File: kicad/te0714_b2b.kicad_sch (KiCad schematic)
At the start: 3 parts

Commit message: WIP
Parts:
- added R1, R11, R12, R13, R14: 10k, Resistor_SMD:R_0603_1608Metric, symbol Device:R_Small
- J5, J6: renamed from J?; footprint MODULE -> Connector_Samtec:Samtec_LSHM-150-xx.x-x-DV-S_2x50-1SH_P0.50mm_Vertical
- gave numbers to parts that had none: 1
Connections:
- net GND: now also J5.SH, J6.SH
- net VCCIO_0: now also R1.2, R11.2, R12.2, R13.2, R14.1
- net B14_L0 renamed IO_L0_14
- net B14_L10_N renamed IO_L10N_14
- net B14_L10_P renamed IO_L10P_14
- net B14_L11_N renamed IO_L11N_14
- net B14_L11_P renamed IO_L11P_14
- net B14_L12_N renamed IO_L12N_14
- net B14_L12_P renamed IO_L12P_14
- net B14_L13_N renamed IO_L13N_14
- net B14_L13_P renamed IO_L13P_14
- net B14_L14_N renamed IO_L14N_14
- net B14_L14_P renamed IO_L14P_14
- net B14_L15_N renamed IO_L15N_14
- net B14_L15_P renamed IO_L15P_14
- net B14_L16_N renamed IO_L16N_14
- net B14_L16_P renamed IO_L16P_14
- net B14_L17_N renamed IO_L17N_14
- net B14_L17_P renamed IO_L17P_14
- net B14_L18_N renamed IO_L18N_14
- net B14_L18_P renamed IO_L18P_14
- net B14_L19_N renamed IO_L19N_14
- net B14_L19_P renamed IO_L19P_14
- net B14_L20_N renamed IO_L20N_14
- net B14_L20_P renamed IO_L20P_14
- net B14_L21_N renamed IO_L21N_14
- net B14_L21_P renamed IO_L21P_14
- net B14_L22_N renamed IO_L22N_14
- net B14_L22_P renamed IO_L22P_14
- net B14_L23_N renamed IO_L23N_14
- net B14_L23_P renamed IO_L23P_14
- net B14_L24_N renamed IO_L24N_14
- net B14_L24_P renamed IO_L24P_14
- net B14_L25 renamed IO_L25_14
- net B14_L4_N renamed IO_L4N_14
- net B14_L4_P renamed IO_L4P_14
- net B14_L5_N renamed IO_L5N_14
- net B14_L5_P renamed IO_L5P_14
- net B14_L7_N renamed IO_L7N_14
- net B14_L7_P renamed IO_L7P_14
- net B14_L8_N renamed IO_L8N_14
- net B14_L8_P renamed IO_L8P_14
- net B14_L9_N renamed IO_L9N_14
- net B14_L9_P renamed IO_L9P_14
- net B15_L10_N renamed IO_L10N_15
- net B15_L10_P renamed IO_L10P_15
- net B15_L11_N renamed IO_L11N_15
- net B15_L11_P renamed IO_L11P_15
- net B15_L12_N renamed IO_L12N_15
- net B15_L12_P renamed IO_L12P_15
- net B15_L13_N renamed IO_L13N_15
- net B15_L13_P renamed IO_L13P_15
- net B15_L14_N renamed IO_L14N_15
- net B15_L14_P renamed IO_L14P_15
- net B15_L15_N renamed IO_L15N_15
- net B15_L15_P renamed IO_L15P_15
- net B15_L16_N renamed IO_L16N_15
- net B15_L16_P renamed IO_L16P_15
- net B15_L17_N renamed IO_L17N_15
- net B15_L17_P renamed IO_L17P_15
- net B15_L18_N renamed IO_L18N_15
- net B15_L18_P renamed IO_L18P_15
- net B15_L19_N renamed IO_L19N_15
- net B15_L19_P renamed IO_L19P_15
- net B15_L1_N renamed IO_L1N_15
- net B15_L1_P renamed IO_L1P_15
- net B15_L20_N renamed IO_L20N_15
- net B15_L20_P renamed IO_L20P_15
- net B15_L21_N renamed IO_L21N_15
- net B15_L21_P renamed IO_L21P_15
- net B15_L22_N renamed IO_L22N_15
- net B15_L22_P renamed IO_L22P_15
- net B15_L23_N renamed IO_L23N_15
- net B15_L23_P renamed IO_L23P_15
- net B15_L24_N renamed IO_L24N_15
- net B15_L24_P renamed IO_L24P_15
- net B15_L2_N renamed IO_L2N_15
- net B15_L2_P renamed IO_L2P_15
- net B15_L3_N renamed IO_L3N_15
- net B15_L3_P renamed IO_L3P_15
- net B15_L4_N renamed IO_L4N_15
- net B15_L4_P renamed IO_L4P_15
- net B15_L5_N renamed IO_L5N_15
- net B15_L5_P renamed IO_L5P_15
- net B15_L6_N renamed IO_L6N_15
- net B15_L6_P renamed IO_L6P_15
- net B15_L7_N renamed IO_L7N_15
- net B15_L7_P renamed IO_L7P_15
- net B15_L8_N renamed IO_L8N_15
- net B15_L8_P renamed IO_L8P_15
- net B15_L9_N renamed IO_L9N_15
- net B15_L9_P renamed IO_L9P_15
- net B34_L10_N renamed IO_L10N_34
- net B34_L10_P renamed IO_L10P_34
- net B34_L11_N renamed IO_L11N_34
- net B34_L11_P renamed IO_L11P_34
- net B34_L12_N renamed IO_L12N_34
- net B34_L12_P renamed IO_L12P_34
- net B34_L13_N renamed IO_L13N_34
- net B34_L13_P renamed IO_L13P_34
- net B34_L14_N renamed IO_L14N_34
- net B34_L14_P renamed IO_L14P_34
- net B34_L15_N renamed IO_L15N_34
- net B34_L15_P renamed IO_L15P_34
- net B34_L16_N renamed IO_L16N_34
- net B34_L16_P renamed IO_L16P_34
- net B34_L17_N renamed IO_L17N_34
- net B34_L17_P renamed IO_L17P_34
- net B34_L18_N renamed IO_L18N_34
- net B34_L18_P renamed IO_L18P_34
- net B34_L19_N renamed IO_L19N_34
- net B34_L19_P renamed IO_L19P_34
- net B34_L1_N renamed IO_L1N_34
- net B34_L1_P renamed IO_L1P_34
- net B34_L20_N renamed IO_L20N_34
- net B34_L20_P renamed IO_L20P_34
- net B34_L21_N renamed IO_L21N_34
- net B34_L21_P renamed IO_L21P_34
- net B34_L22_N renamed IO_L22N_34
- net B34_L22_P renamed IO_L22P_34
- net B34_L23_N renamed IO_L23N_34
- net B34_L23_P renamed IO_L23P_34
- net B34_L24_N renamed IO_L24N_34
- net B34_L24_P renamed IO_L24P_34
- net B34_L2_N renamed IO_L2N_34
- net B34_L2_P renamed IO_L2P_34
- net B34_L3_N renamed IO_L3N_34
- net B34_L3_P renamed IO_L3P_34
- net B34_L4_N renamed IO_L4N_34
- net B34_L4_P renamed IO_L4P_34
- net B34_L5_N renamed IO_L5N_34
- net B34_L5_P renamed IO_L5P_34
- net B34_L6_N renamed IO_L6N_34
- net B34_L6_P renamed IO_L6P_34
- net B34_L7_N renamed IO_L7N_34
- net B34_L7_P renamed IO_L7P_34
- net B34_L8_N renamed IO_L8N_34
- net B34_L8_P renamed IO_L8P_34
- net B34_L9_N renamed IO_L9N_34
- net B34_L9_P renamed IO_L9P_34
- net BOOTMODE: no longer names the net of J6.100
- net SPI-CLK: no longer names the net of J6.67
- net SPI-CS: no longer names the net of J6.69
- net SPI-CS: now also R1.1
- net SPI-DQ1: no longer names the net of J6.71
- net SPI-DQ1: now also R11.1
- net SPI-DQ2: no longer names the net of J6.73
- net SPI-DQ2: now also R12.1
- net SPI-DQ3: no longer names the net of J6.70
- net SPI-DQ3: now also R14.2
- net SPI-DQO: no longer names the net of J6.68
- net SPI-DQO: now also R13.1
- no-connect marks 1 -> 3
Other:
- note added: "BOOTMODE"
- note added: "SPI_CLK"
- note added: "SPI_CS"
- note added: "SPI_D0"
- note added: "SPI_D1"
- note added: "SPI_D2"
- note added: "SPI_D3"

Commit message: basic layout done
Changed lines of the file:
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@@
   (junction (at 119.38 46.99) (diameter 0) (color 0 0 0 0)
-  )
-  (junction (at 241.3 46.99) (diameter 0) (color 0 0 0 0)
   )
   (junction (at 119.38 85.09) (diameter 0) (color 0 0 0 0)
@@
   )
   (wire (pts (xy 49.53 62.23) (xy 66.04 62.23))
-    (stroke (width 0) (type default))
-  )
-  (wire (pts (xy 241.3 46.99) (xy 251.46 46.99))
     (stroke (width 0) (type default))
   )
@@
         )
       )
-    )
-  )
-  (symbol (lib_id "power:PWR_FLAG") (at 251.46 46.99 0) (unit 1)
-    (in_bom yes) (on_board yes) (dnp no)
-    (property "Reference" "#FLG0118" (at 251.46 45.085 0)
-      (effects (font (size 1.27 1.27)) hide)
-    )
-    (property "Value" "PWR_FLAG" (at 251.46 43.4142 0)
-      (effects (font (size 1.27 1.27)))
-    )
-    (property "Footprint" "" (at 251.46 46.99 0)
-      (effects (font (size 1.27 1.27)) hide)
-    )
-    (property "Datasheet" "~" (at 251.46 46.99 0)
-      (effects (font (size 1.27 1.27)) hide)
-    )
-    (pin "1")
-    (instances
-      (project "ecevr-proto"
-        (path "/53719fc4-141e-4c58-98cd-ab3bf9a4e1c0/436aa1dd-06e4-42f7-9e42-2b85da72279f"
-          (reference "#FLG0118") (unit 1)
-        )
-      )

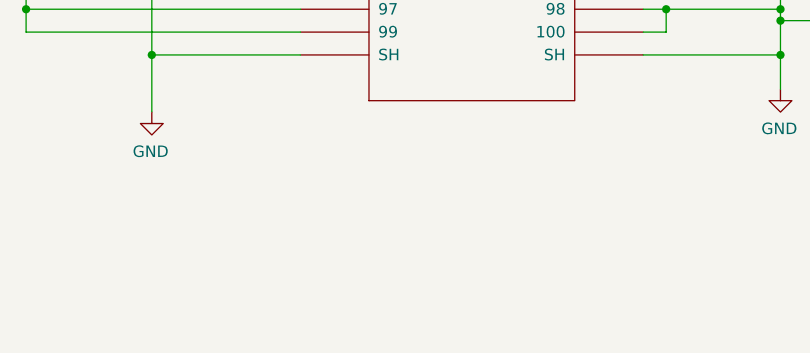
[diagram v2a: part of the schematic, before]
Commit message: First stab. Connected power, added holes and frst clean of silk.
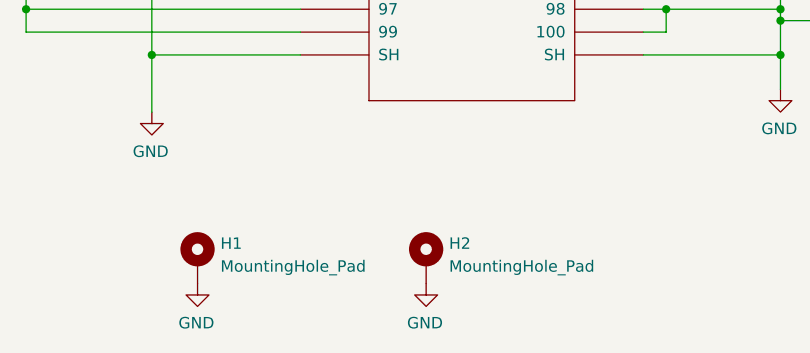
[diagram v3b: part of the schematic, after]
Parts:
- added H1, H2: MountingHole_Pad, MountingHole:MountingHole_3.2mm_M3_DIN965_Pad_TopBottom, symbol Mechanical:MountingHole_Pad
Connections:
- net GND: now also H1.1, H2.1
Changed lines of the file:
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@@
     (effects (font (size 1.27 1.27)) (justify right))
   )
+  (symbol (lib_id "Mechanical:MountingHole_Pad") (at 54.61 176.53 0) (unit 1)
+    (in_bom yes) (on_board yes) (dnp no) (fields_autoplaced)
+    (property "Reference" "H1" (at 57.15 174.625 0)
+      (effects (font (size 1.27 1.27)) (justify left))
+    )
+    (property "Value" "MountingHole_Pad" (at 57.15 177.165 0)
+      (effects (font (size 1.27 1.27)) (justify left))
+    )
+    (property "Footprint" "MountingHole:MountingHole_3.2mm_M3_DIN965_Pad_TopBottom" (at 54.61 176.53 0)
+      (effects (font (size 1.27 1.27)) hide)
+    )
+    (property "Datasheet" "~" (at 54.61 176.53 0)
+      (effects (font (size 1.27 1.27)) hide)
+    )
+    (pin "1")
+    (instances
+      (project "ecevr-proto"
+        (path "/53719fc4-141e-4c58-98cd-ab3bf9a4e1c0/436aa1dd-06e4-42f7-9e42-2b85da72279f"
+          (reference "H1") (unit 1)
+        )
+      )
+    )
+  )
+  (symbol (lib_id "Mechanical:MountingHole_Pad") (at 80.01 176.53 0) (unit 1)
+    (in_bom yes) (on_board yes) (dnp no) (fields_autoplaced)
+    (property "Reference" "H2" (at 82.55 174.625 0)
+      (effects (font (size 1.27 1.27)) (justify left))
+    )
+    (property "Value" "MountingHole_Pad" (at 82.55 177.165 0)
+      (effects (font (size 1.27 1.27)) (justify left))
+    )
+    (property "Footprint" "MountingHole:MountingHole_3.2mm_M3_DIN965_Pad_TopBottom" (at 80.01 176.53 0)
+      (effects (font (size 1.27 1.27)) hide)
+    )
+    (property "Datasheet" "~" (at 80.01 176.53 0)
+      (effects (font (size 1.27 1.27)) hide)
+    )
+    (pin "1")
+    (instances
+      (project "ecevr-proto"
+        (path "/53719fc4-141e-4c58-98cd-ab3bf9a4e1c0/436aa1dd-06e4-42f7-9e42-2b85da72279f"
+          (reference "H2") (unit 1)
+        )
+      )
+    )
+  )
   (symbol (lib_id "Device:R_Small") (at 245.11 113.03 270) (unit 1)
     (in_bom yes) (on_board yes) (dnp no)
@@
     )
   )
+  (symbol (lib_id "power:GND") (at 80.01 179.07 0) (mirror y) (unit 1)
+    (in_bom yes) (on_board yes) (dnp no)
+    (property "Reference" "#PWR03" (at 80.01 185.42 0)
+      (effects (font (size 1.27 1.27)) hide)
+    )
+    (property "Value" "GND" (at 79.883 183.4642 0)
+      (effects (font (size 1.27 1.27)))
+    )
+    (property "Footprint" "" (at 80.01 179.07 0)
+      (effects (font (size 1.27 1.27)) hide)
+    )
+    (property "Datasheet" "" (at 80.01 179.07 0)
+      (effects (font (size 1.27 1.27)) hide)
+    )
+    (pin "1")
+    (instances
+      (project "ecevr-proto"
+        (path "/53719fc4-141e-4c58-98cd-ab3bf9a4e1c0/436aa1dd-06e4-42f7-9e42-2b85da72279f"
+          (reference "#PWR03") (unit 1)
+        )
+      )
+    )
+  )
   (symbol (lib_id "power:PWR_FLAG") (at 154.94 90.17 0) (unit 1)
     (in_bom yes) (on_board yes) (dnp no)
@@
         )
       )
+    )
+  )
+  (symbol (lib_id "power:GND") (at 54.61 179.07 0) (mirror y) (unit 1)
+    (in_bom yes) (on_board yes) (dnp no)
+    (property "Reference" "#PWR02" (at 54.61 185.42 0)
+      (effects (font (size 1.27 1.27)) hide)
+    )
+    (property "Value" "GND" (at 54.483 183.4642 0)
+      (effects (font (size 1.27 1.27)))
+    )
+    (property "Footprint" "" (at 54.61 179.07 0)
+      (effects (font (size 1.27 1.27)) hide)
+    )
+    (property "Datasheet" "" (at 54.61 179.07 0)
+      (effects (font (size 1.27 1.27)) hide)
+    )
+    (pin "1")
+    (instances
+      (project "ecevr-proto"
+        (path "/53719fc4-141e-4c58-98cd-ab3bf9a4e1c0/436aa1dd-06e4-42f7-9e42-2b85da72279f"
+          (reference "#PWR02") (unit 1)
+        )
+      )

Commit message: further work; will need to redo vias :-( for jlcpcb
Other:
- note added: "VCCIO15"
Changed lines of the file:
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@@
+    (effects (font (size 1.27 1.27)) (justify left bottom))
+  )
+  (text "VCCIO15" (at 245.11 92.71 0)
     (effects (font (size 1.27 1.27)) (justify left bottom))
   )
